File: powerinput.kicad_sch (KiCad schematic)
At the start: 1 part, among them J1 Conn_01x03

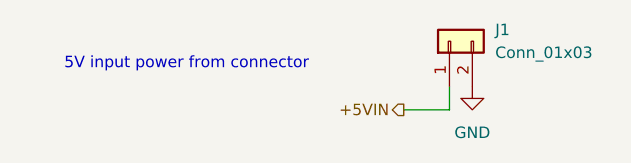
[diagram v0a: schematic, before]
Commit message: Added photodiode circuit.
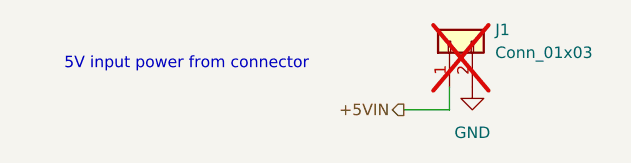
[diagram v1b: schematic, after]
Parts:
- J1: now not fitted; now left out of the parts list
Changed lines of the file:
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@@
 		(body_style 1)
 		(exclude_from_sim no)
-		(in_bom yes)
+		(in_bom no)
 		(on_board yes)
 		(in_pos_files yes)
-		(dnp no)
+		(dnp yes)
 		(fields_autoplaced yes)
 		(property "Reference" "J1"

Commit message: Save progress.
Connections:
- net +5VIN renamed +12VIN
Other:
- note added: "12V input power from connector"
- note removed: "5V input power from connector"
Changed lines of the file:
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@@
 	(generator_version "10.0")
 	(paper "A4")
-	(text "5V input power from connector"
+	(text "12V input power from connector"
 		(exclude_from_sim no)
 		(at 99.06 80.01 0)
@@
 		)
 	)
-	(hierarchical_label "+5VIN"
+	(hierarchical_label "+12VIN"
 		(shape output)
 		(at 123.19 85.09 180)
